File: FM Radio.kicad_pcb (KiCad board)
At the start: 2 copper layers, 53 parts, among them IC1 SI4831-B30-GUR, J1 Conn_01x02_Pin, J2 Conn_01x02_Pin, J3 Conn_01x02_Pin, J4 CONSMA020.062-G, J6 CONSMA020.062-G, SW1 SW_SPDT, SW2 SW_DIP_x01, SW3 SW_Push, SW4 SW_Push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

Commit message: Add comments and fix errors
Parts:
- removed R13, R15: 1k, FM Radio:3362P_1
- removed SW3, SW4: SW_Push, FM Radio:D6R40F1LFS
- added S1: D6R50F1LFS, FM Radio:D6R40F1LFS, F.Cu at (195.3, 89.9)
- added S2: D6R50F1LFS, FM Radio:D6R40F1LFS, F.Cu at (195.3, 105.0)
- added VR1: 3362P-1-102LF, FM Radio:3362P_1, F.Cu at (3.88, 7.09)
- added VR2: 3362P-1-102LF, FM Radio:3362P_1, F.Cu at (12.2, 7.09)
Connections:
- C16 pad 1: Net-(C16-Pad1) -> Net-(IC1-FMI)
- L1 pad 1: Net-(C16-Pad1) -> GND

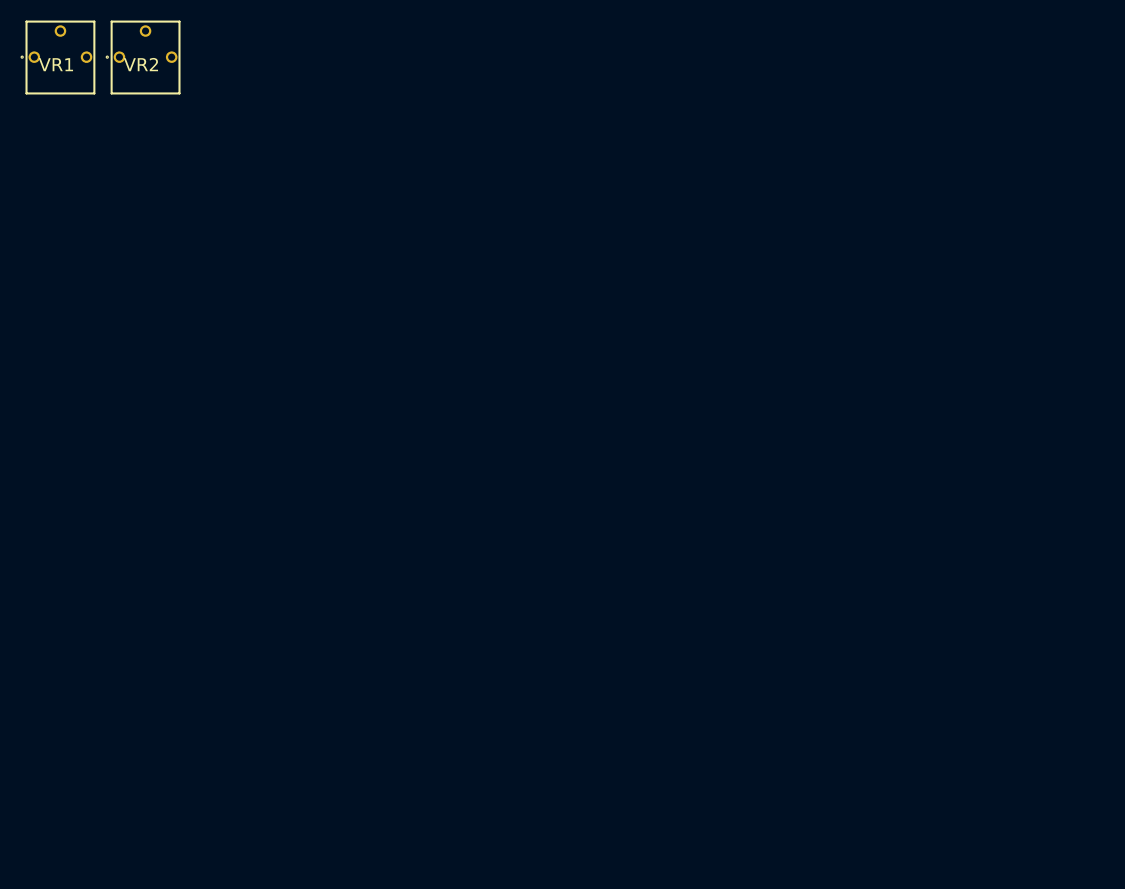
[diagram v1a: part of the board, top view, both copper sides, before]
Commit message: Fix: VDD not connected
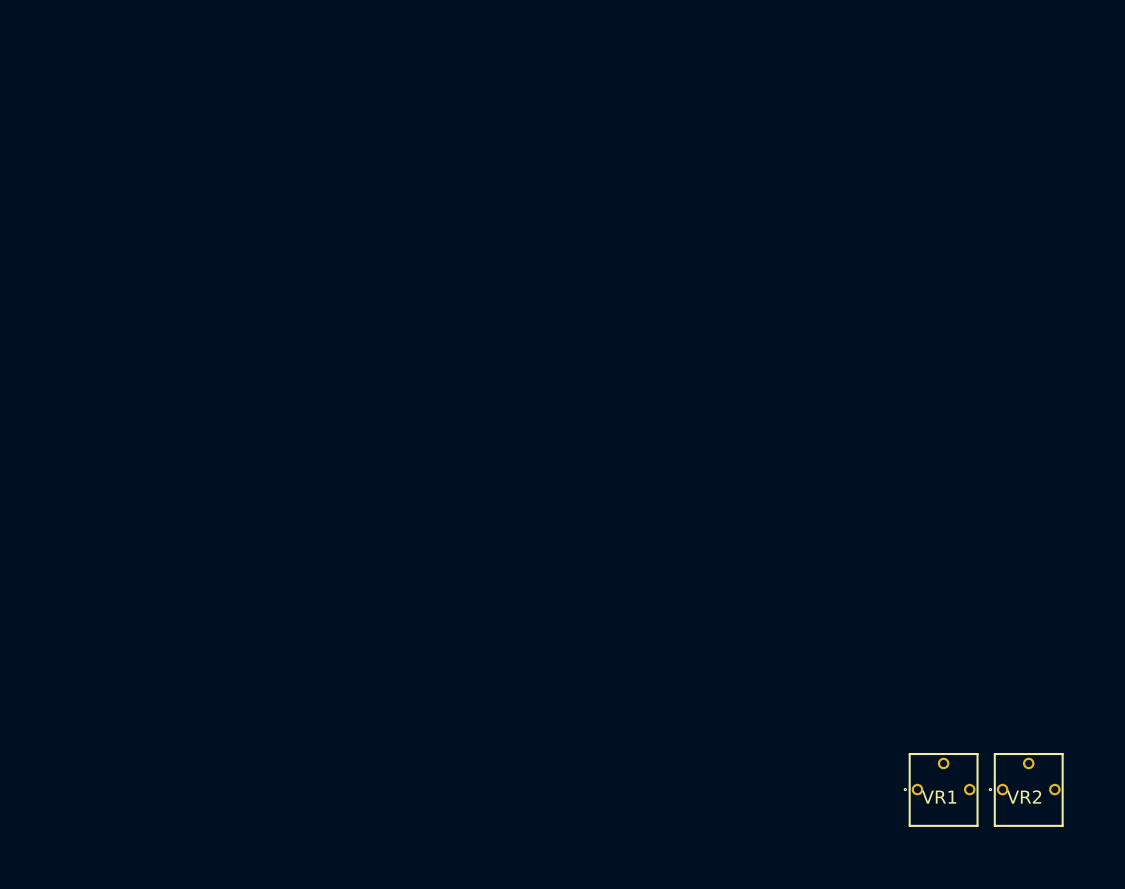
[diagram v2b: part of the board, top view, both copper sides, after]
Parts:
- moved VR1 111.6 mm to (89.8, 78.3)
- moved VR2 111.6 mm to (98.1, 78.3)
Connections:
- IC1 pad 20: Net-(IC1-VDD1) -> +3.3V
- IC1 pad 21: Net-(IC1-VDD1) -> +3.3V
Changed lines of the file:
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@@
   (net 36 "Net-(IC1-VOL+{slash}TREBLE)")
   (net 37 "Net-(IC1-VOL-{slash}BASS)")
-  (net 38 "Net-(IC1-VDD1)")
-  (net 39 "Net-(SW1-C)")
-  (net 40 "Net-(R2-Pad2)")
-  (net 41 "Net-(SW1-A)")
-  (net 42 "Net-(R8-Pad2)")
-  (net 43 "Net-(VR1-CCW)")
-  (net 44 "Net-(VR2-CCW)")
-  (net 45 "unconnected-(U1-BYPASS-Pad7)")
-  (net 46 "unconnected-(U2-BYPASS-Pad7)")
+  (net 38 "Net-(SW1-C)")
+  (net 39 "Net-(R2-Pad2)")
+  (net 40 "Net-(SW1-A)")
+  (net 41 "Net-(R8-Pad2)")
+  (net 42 "Net-(VR1-CCW)")
+  (net 43 "Net-(VR2-CCW)")
+  (net 44 "unconnected-(U1-BYPASS-Pad7)")
+  (net 45 "unconnected-(U2-BYPASS-Pad7)")
   (footprint "FM Radio:RESC1608X55N" (layer "F.Cu")
     (at 141.5425 132.53)
@@
   )
   (footprint "FM Radio:3362P_1" (layer "F.Cu")
-    (at 12.158 7.09)
+    (at 98.06 78.33)
     (descr "3362P")
     (tags "Variable Resistor")
@@
       (stroke (width 0.2) (type solid)) (layer "F.Fab"))
     (pad "1" thru_hole circle (at -2.54 -3.53) (size 1.12 1.12) (drill 0.69) (layers "*.Cu" "*.Mask")
-      (net 44 "Net-(VR2-CCW)") (pinfunction "CCW") (pintype "passive"))
+      (net 43 "Net-(VR2-CCW)") (pinfunction "CCW") (pintype "passive"))
     (pad "2" thru_hole circle (at 0 -6.07) (size 1.12 1.12) (drill 0.69) (layers "*.Cu" "*.Mask")
       (net 20 "Net-(VR2-WIPER)") (pinfunction "WIPER") (pintype "passive"))
@@
       (stroke (width 0.1) (type solid)) (layer "F.Fab"))
     (pad "1" smd rect (at -0.8 0) (size 0.9 0.95) (layers "F.Cu" "F.Paste" "F.Mask")
-      (net 39 "Net-(SW1-C)") (pintype "passive"))
+      (net 38 "Net-(SW1-C)") (pintype "passive"))
     (pad "2" smd rect (at 0.8 0) (size 0.9 0.95) (layers "F.Cu" "F.Paste" "F.Mask")
-      (net 40 "Net-(R2-Pad2)") (pintype "passive"))
+      (net 39 "Net-(R2-Pad2)") (pintype "passive"))
     (model "RK73H1JTTD1003F.stp"
       (offset (xyz 0 0 0))
@@
     (pad "" smd rect (at 3.65 1.43) (size 1 0.8) (layers "F.Cu" "F.Paste" "F.Mask"))
     (pad "1" smd rect (at -2.25 -1.43) (size 0.7 1.5) (layers "F.Cu" "F.Paste" "F.Mask")
-      (net 41 "Net-(SW1-A)") (pinfunction "A") (pintype "passive"))
+      (net 40 "Net-(SW1-A)") (pinfunction "A") (pintype "passive"))
     (pad "2" smd rect (at 0.75 -1.43) (size 0.7 1.5) (layers "F.Cu" "F.Paste" "F.Mask")
       (net 32 "Net-(IC1-BAND)") (pinfunction "B") (pintype "passive"))
     (pad "3" smd rect (at 2.25 -1.43) (size 0.7 1.5) (layers "F.Cu" "F.Paste" "F.Mask")
-      (net 39 "Net-(SW1-C)") (pinfunction "C") (pintype "passive"))
+      (net 38 "Net-(SW1-C)") (pinfunction "C") (pintype "passive"))
     (model "${KICAD6_3DMODEL_DIR}/Button_Switch_SMD.3dshapes/SW_SPDT_PCM12.wrl"
       (offset (xyz 0 0 0))
@@
       (net 2 "+3.3V") (pintype "passive"))
     (pad "2" smd roundrect (at 0.9125 0) (size 0.975 0.95) (layers "F.Cu" "F.Paste" "F.Mask") (roundrect_rratio 0.25)
-      (net 42 "Net-(R8-Pad2)") (pintype "passive"))
+      (net 41 "Net-(R8-Pad2)") (pintype "passive"))
     (model "${KICAD6_3DMODEL_DIR}/Resistor_SMD.3dshapes/R_0603_1608Metric.wrl"
       (offset (xyz 0 0 0))
@@
       (stroke (width 0.1) (type solid)) (layer "F.Fab"))
     (pad "1" smd roundrect (at -2.475 -1.905) (size 1.95 0.6) (layers "F.Cu" "F.Paste" "F.Mask") (roundrect_rratio 0.25)
-      (net 43 "Net-(VR1-CCW)") (pinfunction "GAIN") (pintype "input"))
+      (net 42 "Net-(VR1-CCW)") (pinfunction "GAIN") (pintype "input"))
     (pad "2" smd roundrect (at -2.475 -0.635) (size 1.95 0.6) (layers "F.Cu" "F.Paste" "F.Mask") (roundrect_rratio 0.25)
       (net 4 "GND") (pinfunction "-") (pintype "input"))
@@
       (net 11 "+9V") (pinfunction "V+") (pintype "power_in"))
     (pad "7" smd roundrect (at 2.475 -0.635) (size 1.95 0.6) (layers "F.Cu" "F.Paste" "F.Mask") (roundrect_rratio 0.25)
-      (net 45 "unconnected-(U1-BYPASS-Pad7)") (pinfunction "BYPASS") (pintype "input+no_connect"))
+      (net 44 "unconnected-(U1-BYPASS-Pad7)") (pinfunction "BYPASS") (pintype "input+no_connect"))
     (pad "8" smd roundrect (at 2.475 -1.905) (size 1.95 0.6) (layers "F.Cu" "F.Paste" "F.Mask") (roundrect_rratio 0.25)
       (net 19 "Net-(C14-Pad2)") (pinfunction "GAIN") (pintype "input"))
@@
       (net 30 "Net-(IC1-TUNE1)") (pintype "passive"))
     (pad "2" smd rect (at 0.8 0) (size 0.9 0.95) (layers "F.Cu" "F.Paste" "F.Mask")
-      (net 41 "Net-(SW1-A)") (pintype "passive"))
+      (net 40 "Net-(SW1-A)") (pintype "passive"))
     (model "RK73H1JTTD1003F.stp"
       (offset (xyz 0 0 0))
@@
       (stroke (width 0.1) (type solid)) (layer "F.Fab"))
     (pad "1" smd roundrect (at -2.475 -1.905) (size 1.95 0.6) (layers "F.Cu" "F.Paste" "F.Mask") (roundrect_rratio 0.25)
-      (net 44 "Net-(VR2-CCW)") (pinfunction "GAIN") (pintype "input"))
+      (net 43 "Net-(VR2-CCW)") (pinfunction "GAIN") (pintype "input"))
     (pad "2" smd roundrect (at -2.475 -0.635) (size 1.95 0.6) (layers "F.Cu" "F.Paste" "F.Mask") (roundrect_rratio 0.25)
       (net 4 "GND") (pinfunction "-") (pintype "input"))
@@
       (net 11 "+9V") (pinfunction "V+") (pintype "power_in"))
     (pad "7" smd roundrect (at 2.475 -0.635) (size 1.95 0.6) (layers "F.Cu" "F.Paste" "F.Mask") (roundrect_rratio 0.25)
-      (net 46 "unconnected-(U2-BYPASS-Pad7)") (pinfunction "BYPASS") (pintype "input+no_connect"))
+      (net 45 "unconnected-(U2-BYPASS-Pad7)") (pinfunction "BYPASS") (pintype "input+no_connect"))
     (pad "8" smd roundrect (at 2.475 -1.905) (size 1.95 0.6) (layers "F.Cu" "F.Paste" "F.Mask") (roundrect_rratio 0.25)
       (net 21 "Net-(C15-Pad2)") (pinfunction "GAIN") (pintype "input"))
@@
       (stroke (width 0.1) (type solid)) (layer "F.Fab"))
     (pad "1" smd rect (at -0.8 0) (size 0.9 0.95) (layers "F.Cu" "F.Paste" "F.Mask")
-      (net 40 "Net-(R2-Pad2)") (pintype "passive"))
+      (net 39 "Net-(R2-Pad2)") (pintype "passive"))
     (pad "2" smd rect (at 0.8 0) (size 0.9 0.95) (layers "F.Cu" "F.Paste" "F.Mask")
       (net 4 "GND") (pintype "passive"))
@@
       (stroke (width 0.1) (type solid)) (layer "F.Fab"))
     (pad "1" smd rect (at -0.8 0) (size 0.9 0.95) (layers "F.Cu" "F.Paste" "F.Mask")
-      (net 41 "Net-(SW1-A)") (pintype "passive"))
+      (net 40 "Net-(SW1-A)") (pintype "passive"))
     (pad "2" smd rect (at 0.8 0) (size 0.9 0.95) (layers "F.Cu" "F.Paste" "F.Mask")
-      (net 39 "Net-(SW1-C)") (pintype "passive"))
+      (net 38 "Net-(SW1-C)") (pintype "passive"))
     (model "RK73H1JTTD1003F.stp"
       (offset (xyz 0 0 0))
@@
       (net 27 "Net-(D2-K)") (pintype "passive"))
     (pad "2" thru_hole circle (at 0 -7.62) (size 1.575 1.575) (drill 1.05) (layers "*.Cu" "*.Mask")
-      (net 42 "Net-(R8-Pad2)") (pintype "passive"))
+      (net 41 "Net-(R8-Pad2)") (pintype "passive"))
     (model "DS01-254-L-01BE.stp"
       (offset (xyz -2.650000056 3.799999895 1.350000004))
@@
   )
   (footprint "FM Radio:3362P_1" (layer "F.Cu")
-    (at 3.879 7.09)
+    (at 89.781 78.33)
     (descr "3362P")
     (tags "Variable Resistor")
@@
       (stroke (width 0.2) (type solid)) (layer "F.Fab"))
     (pad "1" thru_hole circle (at -2.54 -3.53) (size 1.12 1.12) (drill 0.69) (layers "*.Cu" "*.Mask")
-      (net 43 "Net-(VR1-CCW)") (pinfunction "CCW") (pintype "passive"))
+      (net 42 "Net-(VR1-CCW)") (pinfunction "CCW") (pintype "passive"))
     (pad "2" thru_hole circle (at 0 -6.07) (size 1.12 1.12) (drill 0.69) (layers "*.Cu" "*.Mask")
       (net 18 "Net-(VR1-WIPER)") (pinfunction "WIPER") (pintype "passive"))
@@
       (net 6 "Net-(IC1-XTALI)") (pinfunction "XTALI") (pintype "passive"))
     (pad "20" smd rect (at 2.7 -0.952 90) (size 0.435 1.5) (layers "F.Cu" "F.Paste" "F.Mask")
-      (net 38 "Net-(IC1-VDD1)") (pinfunction "VDD1") (pintype "passive"))
+      (net 2 "+3.3V") (pinfunction "VDD1") (pintype "passive"))
     (pad "21" smd rect (at 2.7 -1.588 90) (size 0.435 1.5) (layers "F.Cu" "F.Paste" "F.Mask")
-      (net 38 "Net-(IC1-VDD1)") (pinfunction "VDD2") (pintype "passive"))
+      (net 2 "+3.3V") (pinfunction "VDD2") (pintype "passive"))
     (pad "22" smd rect (at 2.7 -2.222 90) (size 0.435 1.5) (layers "F.Cu" "F.Paste" "F.Mask")
       (net 1 "Net-(IC1-DBYP)") (pinfunction "DBYP") (pintype "passive"))

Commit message: Very rough component placement
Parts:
- added C18: 0.1u, Capacitor_SMD:C_0603_1608Metric, F.Cu at (133.3, 76.5)
- added C19: 0.1u, Capacitor_SMD:C_0603_1608Metric, F.Cu at (133.7, 94.5)
- moved C14 61.1 mm to (130.1, 76.4)
- moved J4 58.7 mm to (188.4, 116.7)
- moved C10 56.7 mm to (138.5, 73.4), turned to 90 degrees
- moved J1 56.7 mm to (116.9, 73.9), turned to 90 degrees
- moved R14 53.9 mm to (140.3, 81.2), turned to -90 degrees
- moved SW2 53.1 mm to (192.3, 85.6), turned to 180 degrees
- moved C13 52.2 mm to (143.9, 82.9)
- moved U3 49.1 mm to (173.3, 72.4)
- moved C17 48.8 mm to (185.4, 104.7)
- moved C11 47.9 mm to (136.8, 90.3)
- moved U1 46.3 mm to (134.7, 81.2), turned to 90 degrees
- moved C15 45.3 mm to (130.5, 94.5)
- moved J2 44.5 mm to (116.9, 90.4), turned to 90 degrees
- moved J6 43.7 mm to (168.3, 116.6)
- moved Y1 42.3 mm to (167.5, 87.9)
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- renumbered C5 to 0.1u, C1 to 4.7u
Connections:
- VR1 pad 3: GND -> unconnected-(VR1-CW-Pad3)
- VR2 pad 3: GND -> unconnected-(VR2-CW-Pad3)
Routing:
- net +3.3V: track 0.00 -> 4.26 mm
- net Net-(IC1-DBYP): track 0.00 -> 3.74 mm

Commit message: Complete layout
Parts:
- added ?: , , B.Cu at (183.4, 98.0)
- added ?: , , B.Cu at (165.2, 113.6)
- added ?: , , B.Cu at (173.7, 113.6)
- added ?: , , B.Cu at (183.4, 89.5)
- added G***: LOGO, LOGO, F.Cu at (118.2, 70.7)
- R1, R10, R11, R12, R14, R2, R3, R4, R5, R9: footprint FM Radio:RESC1608X55N -> Resistor_SMD:R_0603_1608Metric
- moved RV1 54.9 mm to (119.6, 105.0), turned to -90 degrees
- moved SW2 51.3 mm to (145.8, 107.3), turned to -90 degrees
- moved J3 45.5 mm to (153.8, 75.9), turned to 180 degrees
- moved S2 45.3 mm to (161.2, 78.2), turned to 90 degrees
- moved S1 42.3 mm to (176.3, 78.2), turned to 90 degrees
- moved U3 26.8 mm to (146.8, 76.1), turned to 90 degrees
- moved C9 24.8 mm to (142.3, 74.3), turned to 90 degrees
- moved J4 23.0 mm to (188.1, 93.7), turned to 90 degrees
- moved D5 20.8 mm to (173.4, 92.8), turned to 180 degrees
- moved D3 19.1 mm to (146.8, 83.5), turned to 90 degrees
- moved R9 16.9 mm to (174.0, 85.0)
- moved C8 16.7 mm to (151.5, 80.7), turned to 90 degrees
- moved R11 16.5 mm to (145.1, 83.5), turned to 90 degrees
- moved C17 14.6 mm to (173.7, 95.9)
- moved R3 13.9 mm to (160.3, 101.4)
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- renumbered 4.7u to C1, 0.1u to C5
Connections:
- net Net-(D4-CH1) renamed /FM_ANT
- net Net-(D5-CH1) renamed /AM_ANT
- C14 pad 1: Net-(VR1-WIPER) -> Net-(VR1-CW)
- C15 pad 1: Net-(VR2-WIPER) -> Net-(VR2-CW)
- VR1 pad 2: Net-(VR1-WIPER) -> Net-(VR1-CW)
- VR1 pad 3: unconnected-(VR1-CW-Pad3) -> Net-(VR1-CW)
- VR2 pad 2: Net-(VR2-WIPER) -> Net-(VR2-CW)
- VR2 pad 3: unconnected-(VR2-CW-Pad3) -> Net-(VR2-CW)
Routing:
- net +3.3V: track 4.26 -> 104.0 mm
- net Net-(IC1-TUNE1): track 0.00 -> 55.8 mm
- net Net-(IC1-TUNE2): track 0.00 -> 53.5 mm
- net +9V: track 0.00 -> 43.4 mm, vias 0 -> 3
- net GND: track 0.00 -> 33.9 mm, vias 0 -> 102
- net Net-(IC1-VOL-/BASS): track 0.00 -> 33.8 mm
- net Net-(IC1-VOL+/TREBLE): track 0.00 -> 33.6 mm
- net Net-(D2-K): track 0.00 -> 16.7 mm
- net Net-(IC1-AMI): track 0.00 -> 13.5 mm
- net Net-(IC1-FMI): track 0.00 -> 12.0 mm
- net Net-(IC1-ROUT): track 0.00 -> 10.8 mm
- net /LM386/LOUT: track 0.00 -> 10.4 mm
- net Net-(IC1-BAND): track 0.00 -> 9.96 mm
- net /LM386/ROUT: track 0.00 -> 9.78 mm
- net Net-(IC1-~{RST}): track 0.00 -> 9.01 mm
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- added copper zone on F.Cu, net +3.3V
- added copper zone on F.Cu, net +9V
- added copper zone on F.Cu, net /AM_ANT
- added copper zone on F.Cu, net /FM_ANT
- added copper zone on B.Cu, net GND
- added copper zone on F.Cu, net GND
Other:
- board outline added: 72.7 x 49.9 mm
- board text added: "+9V"
- board text added: "AM/FM"
- board text added: "AM_ANT"
- board text added: "FM Radio"
- board text added: "FM_ANT"
- board text added: "GND"
- board text added: "LOUT"
- board text added: "ROUT"
- board text added: "Yifan, 2024-02-04"
- board text added: "←Bass/Treble →Volume"
- board text added: "↑"
- board text added: "↓"

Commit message: Plot Gerber
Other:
- board text added: "AM/FM Radio"
- board text removed: "FM Radio"
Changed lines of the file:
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@@
       (usegerberattributes true)
       (usegerberadvancedattributes true)
-      (creategerberjobfile true)
+      (creategerberjobfile false)
       (dashed_line_dash_ratio 12.000000)
       (dashed_line_gap_ratio 3.000000)
@@
       (outputformat 1)
       (mirror false)
-      (drillshape 1)
+      (drillshape 0)
       (scaleselection 1)
-      (outputdirectory "")
+      (outputdirectory "Gerber/")
     )
   )
@@
     (effects (font (size 1.5 1.5) (thickness 0.25)) (justify left bottom mirror))
   )
-  (gr_text "FM Radio" (at 121.43 71.82) (layer "F.SilkS")
+  (gr_text "AM/FM Radio" (at 121.43 71.82) (layer "F.SilkS")
     (effects (font (size 1.5 1.5) (thickness 0.15)) (justify left bottom))
   )
